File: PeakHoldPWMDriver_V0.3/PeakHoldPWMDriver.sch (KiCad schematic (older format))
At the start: 105 parts, among them J1 Screw_Terminal_01x06, J2 Screw_Terminal_01x08, Q1 AO3400, Q10 AO3400, Q11 2N7002, Q12 2N7002, Q13 TSM2309, Q14 IRLL 024N, Q15 TSM2309, Q16 IRLL 024N, Q2 AO3400, Q3 2N7002, Q4 2N7002, Q5 TSM2309, Q6 TSM2309, Q7 IRLL 024N, Q8 IRLL 024N, Q9 AO3400, U1 74LS32, U2 LM2901, U3 74LS74, U4 LTC6992, U5 74LS74, U6 LM78M05, U7 74LS08, U8 74LS08

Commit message: cleaup
cleanup of silkscreen
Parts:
- R3: value 500k -> 470k
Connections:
- net PWR_GND: now also RV1.1, RV2.1; no longer RV1.3, RV2.3
- net at D4.2 (A), R6.2: now also RV2.3; no longer RV2.1
- net at D1.2 (A), R2.2: now also RV1.3; no longer RV1.1
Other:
- moved on the sheet: D1, R2, RV2
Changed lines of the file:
@@
 L Device:R_Small R2
 U 1 1 5F079FC0
-P 1350 6300
-F 0 "R2" H 1409 6346 50  0000 L CNN
-F 1 "470R" H 1409 6255 50  0000 L CNN
-F 2 "Resistor_SMD:R_0603_1608Metric_Pad1.05x0.95mm_HandSolder" H 1350 6300 50  0001 C CNN
-F 3 "~" H 1350 6300 50  0001 C CNN
-	1    1350 6300
-	1    0    0    -1
-$EndComp
-Wire Wire Line
-	1350 6400 1350 6450
-Text GLabel 1250 6150 0    50   Input ~ 0
+P 1050 6800
+F 0 "R2" H 1109 6846 50  0000 L CNN
+F 1 "470R" H 1109 6755 50  0000 L CNN
+F 2 "Resistor_SMD:R_0603_1608Metric_Pad1.05x0.95mm_HandSolder" H 1050 6800 50  0001 C CNN
+F 3 "~" H 1050 6800 50  0001 C CNN
+	1    1050 6800
+	-1   0    0    1
+$EndComp
+Wire Wire Line
+	1050 6700 1050 6650
+Text GLabel 1150 6950 2    50   Input ~ 0
 5V
 Wire Wire Line
-	1250 6150 1350 6150
-Wire Wire Line
-	1350 6150 1350 6200
-Wire Wire Line
-	1350 6650 1350 6700
-Wire Wire Line
-	1350 6700 1250 6700
+	1150 6950 1050 6950
+Wire Wire Line
+	1050 6950 1050 6900
 $Comp
 L Device:R_POT_Small RV1
@@
 $EndComp
 Wire Wire Line
-	1350 6450 1700 6450
-Connection ~ 1350 6450
-Wire Wire Line
-	1350 6700 1550 6700
-Wire Wire Line
-	1700 6700 1700 6650
-Connection ~ 1350 6700
-Wire Wire Line
 	1800 6600 1800 6550
 $Comp
@@
 P 1750 6750
 F 0 "R3" H 1600 6800 42  0000 L BNN
-F 1 "500k" H 1600 6650 42  0000 L BNN
+F 1 "470k" H 1600 6650 42  0000 L BNN
 F 2 "Resistor_SMD:R_0603_1608Metric_Pad1.05x0.95mm_HandSolder" H 1750 6750 50  0001 C CNN
 F 3 "" H 1750 6750 50  0001 C CNN
@@
 Wire Wire Line
 	1900 6700 1900 6750
-Wire Wire Line
-	1600 6750 1550 6750
-Wire Wire Line
-	1550 6750 1550 6700
-Connection ~ 1550 6700
-Wire Wire Line
-	1550 6700 1700 6700
 $Comp
 L Speeduino_base-eagle-import:SMD-RES-470R-5%-1_10W(0603) R4
@@
 L Device:D_Schottky_Small D1
 U 1 1 5F079FBA
-P 1350 6550
-F 0 "D1" H 1350 6437 50  0000 C CNN
-F 1 "BAV103" V 1395 6618 50  0001 L CNN
-F 2 "Diode_SMD:D_MiniMELF" V 1350 6550 50  0001 C CNN
-F 3 "~" V 1350 6550 50  0001 C CNN
-	1    1350 6550
-	0    -1   -1   0
+P 1050 6550
+F 0 "D1" H 1050 6437 50  0000 C CNN
+F 1 "BAV103" V 1095 6618 50  0001 L CNN
+F 2 "Diode_SMD:D_MiniMELF" V 1050 6550 50  0001 C CNN
+F 3 "~" V 1050 6550 50  0001 C CNN
+	1    1050 6550
+	0    1    1    0
 $EndComp
 $Comp
@@
 Text GLabel 3050 6600 2    50   Output ~ 0
 PWM
-Text GLabel 3900 6750 2    50   Output ~ 0
+Text GLabel 3800 6750 0    50   Output ~ 0
 VREF
 Connection ~ 3450 6900
@@
 	3450 6900 3800 6900
 Connection ~ 3450 6650
-Wire Wire Line
-	3450 6650 3800 6650
 $Comp
 L Device:R_POT_Small RV2
 U 1 1 5EDE3906
-P 3800 6750
-F 0 "RV2" H 3741 6796 50  0000 R CNN
-F 1 "5K" H 3741 6705 50  0000 R CNN
-F 2 "Potentiometer_SMD:Potentiometer_Bourns_3314R-1_Vertical_Hole" H 3800 6750 50  0001 C CNN
-F 3 "~" H 3800 6750 50  0001 C CNN
-	1    3800 6750
-	1    0    0    -1
+P 3900 6750
+F 0 "RV2" H 3841 6796 50  0000 R CNN
+F 1 "5K" H 3841 6705 50  0000 R CNN
+F 2 "Potentiometer_SMD:Potentiometer_Bourns_3314R-1_Vertical_Hole" H 3900 6750 50  0001 C CNN
+F 3 "~" H 3900 6750 50  0001 C CNN
+	1    3900 6750
+	-1   0    0    1
 $EndComp
 Wire Wire Line
@@
 Text GLabel 3350 6900 0    50   Input ~ 0
 PWR_GND
-Text GLabel 1250 6700 0    50   Input ~ 0
+Text GLabel 1050 6350 1    50   Input ~ 0
 PWR_GND
 Text GLabel 4400 5200 2    50   Input ~ 0
@@
 Wire Wire Line
 	10000 4500 10050 4500
+Wire Wire Line
+	3450 6650 3900 6650
+Wire Wire Line
+	3800 6850 3900 6850
+Text GLabel 1550 6800 3    50   Input ~ 0
+PWR_GND
+Wire Wire Line
+	1550 6800 1550 6750
+Wire Wire Line
+	1550 6750 1600 6750
+Wire Wire Line
+	1050 6350 1050 6400
+Wire Wire Line
+	1050 6400 1700 6400
+Wire Wire Line
+	1700 6400 1700 6450
+Connection ~ 1050 6400
+Wire Wire Line
+	1050 6400 1050 6450
+Wire Wire Line
+	1050 6650 1700 6650
+Connection ~ 1050 6650
 $EndSCHEMATC

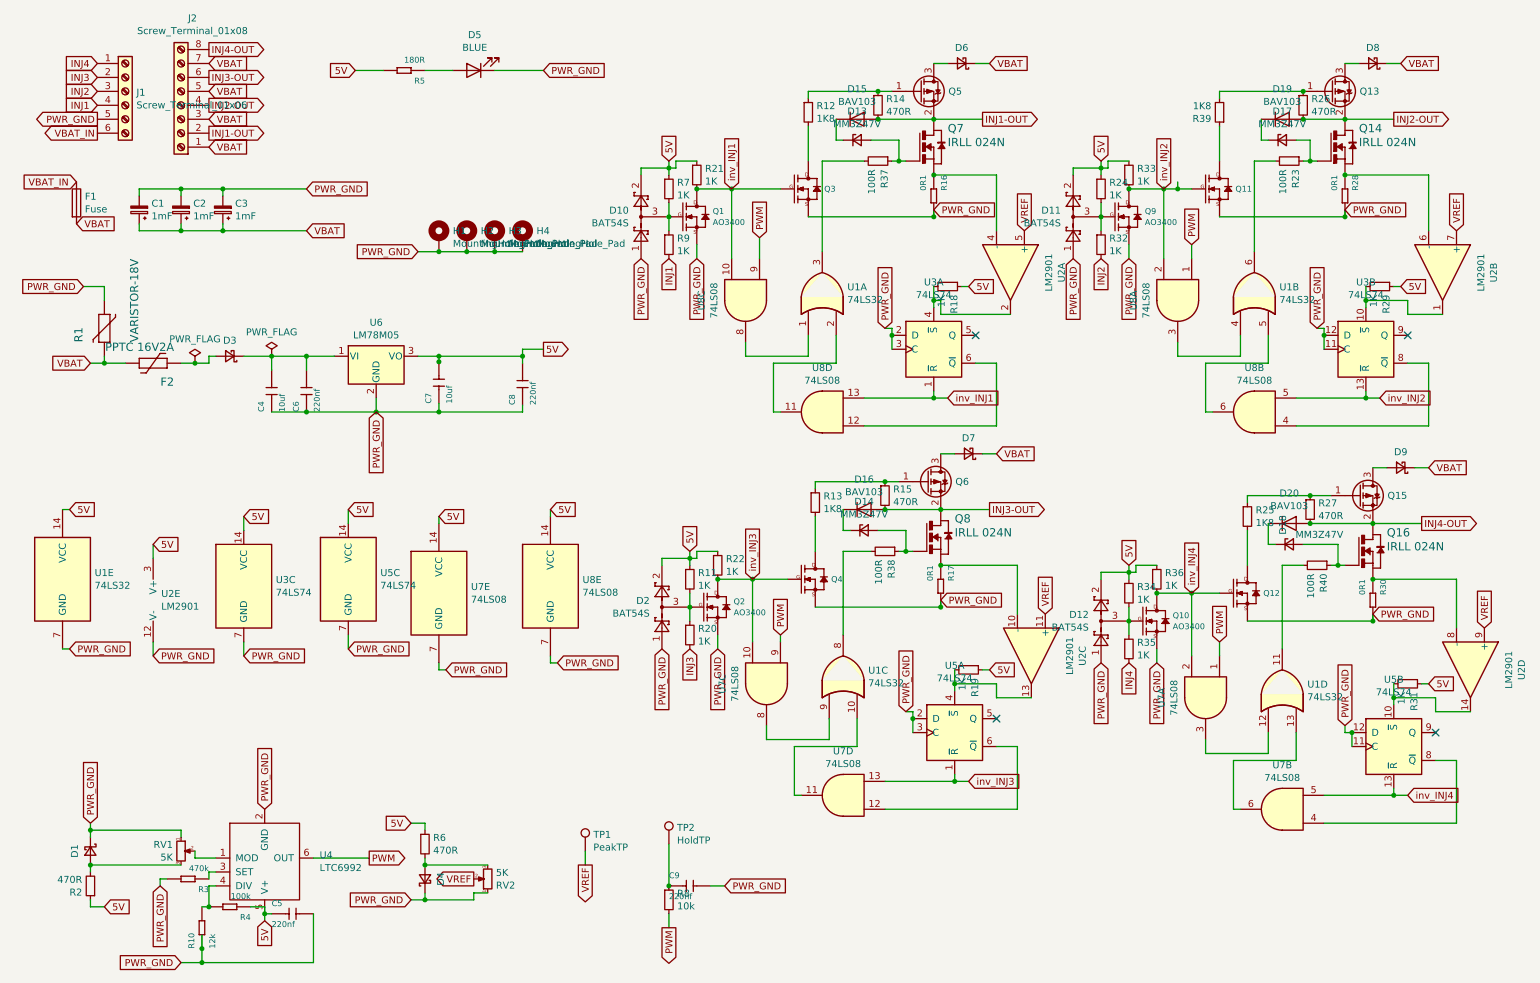
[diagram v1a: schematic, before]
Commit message: Added jumpers to choose between ECU or transistor input
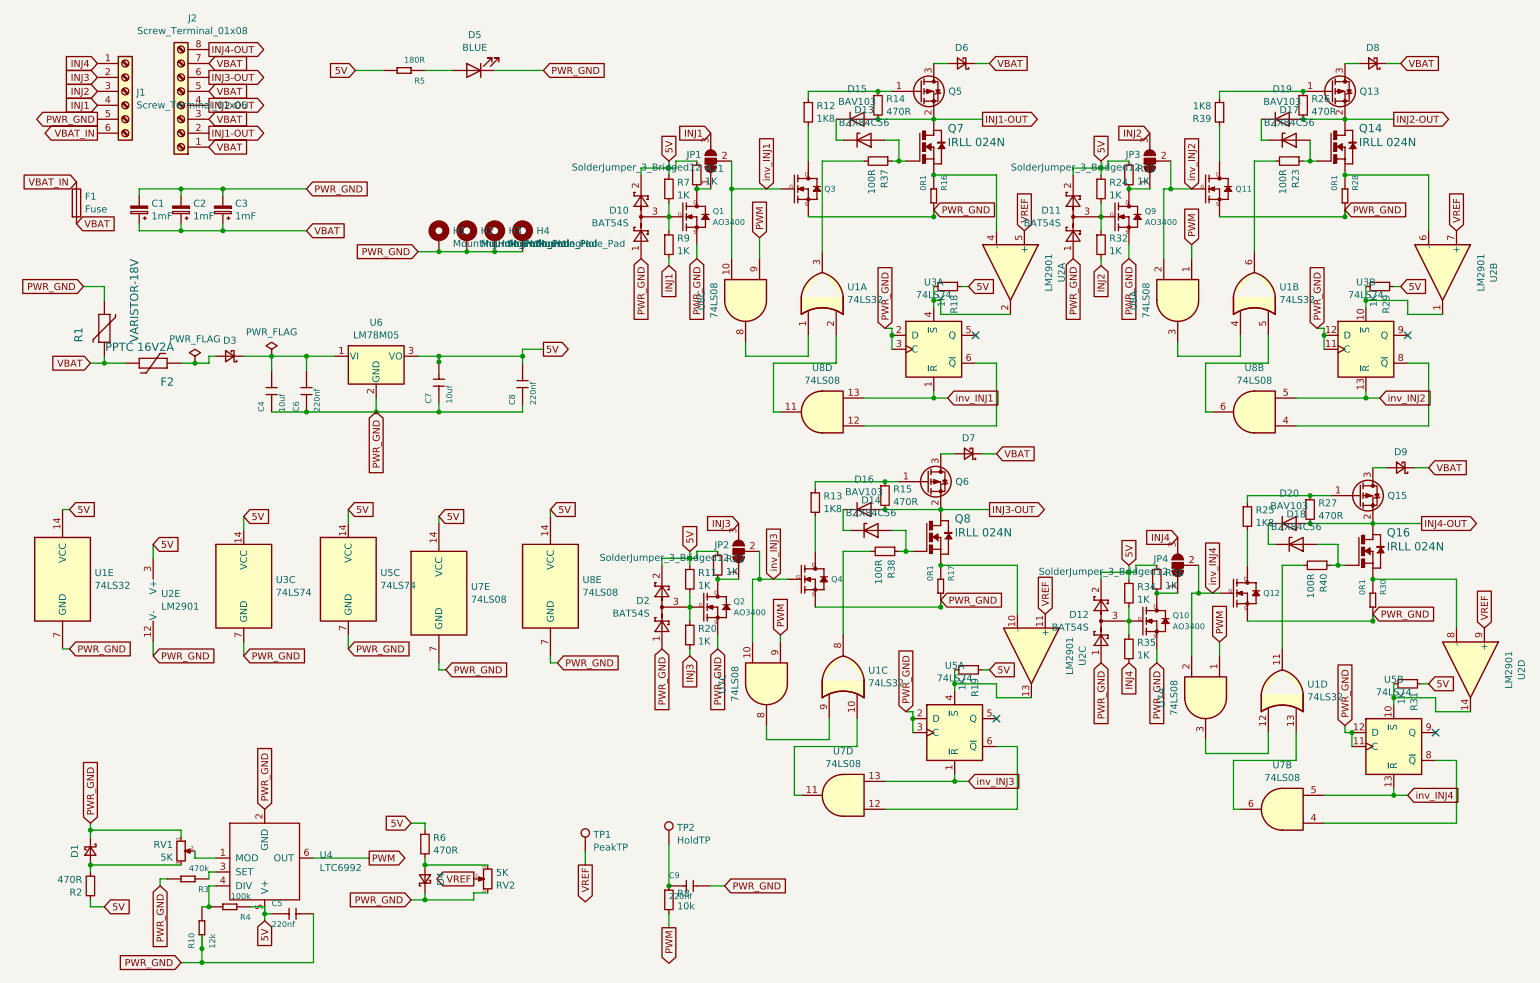
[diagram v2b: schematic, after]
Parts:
- removed D13, D14, D17, D18: MM3Z47V, Diode_SMD:D_SOD-323, symbol Device:D_Zener_Small
- added D13, D14, D17, D18: BZX84C56, Diode_SMD:D_SOT-23_ANK, symbol Diode:BZX84Cxx
- added JP1, JP2, JP3, JP4: SolderJumper_3_Bridged12, Jumper:SolderJumper-3_P1.3mm_Bridged12_Pad1.0x1.5mm, symbol Jumper:SolderJumper_3_Bridged12
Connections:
- net INJ1: now also JP1.3 (B)
- net INJ2: now also JP3.3 (B)
- net INJ3: now also JP2.3 (B)
- net INJ4: now also JP4.3 (B)
- net inv_INJ1: now also JP1.2 (C); no longer Q1.3 (D), R21.2
- net inv_INJ2: now also JP3.2 (C); no longer Q9.3 (D), R33.2
- net inv_INJ3: now also JP2.2 (C); no longer Q2.3 (D), R22.2
- net inv_INJ4: now also JP4.2 (C); no longer Q10.3 (D), R36.2
- net at Q8.1 (G), R38.1: now also D14.2 (A)
- net at Q14.1 (G), R23.1: now also D17.2 (A)
- net at Q16.1 (G), R40.1: now also D18.2 (A)
- net at Q7.1 (G), R37.1: now also D13.2 (A)
- net at D16.1 (K): now also D14.1 (K)
- net at D15.1 (K): now also D13.1 (K)
- net at D19.1 (K): now also D17.1 (K)
- net at D20.1 (K): now also D18.1 (K)
- new net: JP1.1 (A), Q1.3 (D), R21.2
- new net: JP2.1 (A), Q2.3 (D), R22.2
- new net: JP4.1 (A), Q10.3 (D), R36.2
- new net: JP3.1 (A), Q9.3 (D), R33.2
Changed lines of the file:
@@
 Wire Wire Line
 	6200 1150 6200 1100
-Text GLabel 5650 1800 1    50   Input ~ 0
+Text GLabel 5900 1800 1    50   Input ~ 0
 inv_INJ1
 Wire Wire Line
@@
 Wire Wire Line
 	6250 3950 6250 3900
-Text GLabel 5800 4600 1    50   Input ~ 0
+Text GLabel 5950 4600 1    50   Input ~ 0
 inv_INJ3
 Text GLabel 10050 1950 2    50   Input ~ 0
@@
 Wire Wire Line
 	9150 1100 9750 1100
-Wire Wire Line
-	8850 1750 8850 1800
-Wire Wire Line
-	8850 1800 8950 1800
-Wire Wire Line
-	8850 1800 8750 1800
-Connection ~ 8850 1800
-Text GLabel 8750 1800 1    50   Input ~ 0
+Text GLabel 8950 1800 1    50   Input ~ 0
 inv_INJ2
 Text GLabel 10250 4850 2    50   Input ~ 0
@@
 Wire Wire Line
 	9350 4050 9350 4000
-Text GLabel 8950 4700 1    50   Input ~ 0
+Text GLabel 9100 4700 1    50   Input ~ 0
 inv_INJ4
 Text GLabel 10450 900  2    50   Input ~ 0
@@
 Text GLabel 5000 2300 3    50   Input ~ 0
 PWR_GND
-Text GLabel 5200 2300 3    50   Input ~ 0
-INJ1
 Text GLabel 1100 1200 0    50   Input ~ 0
 INJ1
@@
 	1850 7350 2650 7350
 Wire Wire Line
-	5800 4600 6050 4600
+	5800 4600 5850 4600
 Wire Wire Line
 	5650 1800 6000 1800
@@
 	5400 2200 5400 2300
 Wire Wire Line
-	5400 1800 5650 1800
-Wire Wire Line
 	5200 2000 5200 2100
 Wire Wire Line
@@
 	1    0    0    -1
 $EndComp
-Connection ~ 5650 1800
 Wire Wire Line
 	5000 1700 5000 1650
@@
 	8950 4700 8950 5150
 Wire Wire Line
-	8950 4700 9150 4700
+	8950 4700 9000 4700
 $Comp
 L Device:R_Small R21
@@
 	1    0    0    -1
 $EndComp
-Connection ~ 5400 1800
 Wire Wire Line
 	5400 1600 5250 1600
@@
 Text GLabel 5150 5100 3    50   Input ~ 0
 PWR_GND
-Text GLabel 5350 5100 3    50   Input ~ 0
+Text GLabel 5350 5150 3    50   Input ~ 0
 INJ3
 $Comp
@@
 	5550 5000 5550 5100
 Wire Wire Line
-	5550 4600 5800 4600
-Wire Wire Line
 	5350 4800 5350 4900
 Wire Wire Line
@@
 	1    0    0    -1
 $EndComp
-Connection ~ 5550 4600
 Wire Wire Line
 	5550 4400 5400 4400
@@
 	1    0    0    -1
 $EndComp
-Connection ~ 5800 4600
 Text GLabel 8300 5200 3    50   Input ~ 0
 PWR_GND
@@
 	8700 5100 8700 5200
 Wire Wire Line
-	8700 4700 8950 4700
-Wire Wire Line
 	8500 4900 8500 5000
 Wire Wire Line
@@
 	1    0    0    -1
 $EndComp
-Connection ~ 8700 4700
 Wire Wire Line
 	8700 4500 8550 4500
@@
 	1    0    0    -1
 $EndComp
-Connection ~ 8950 4700
 Wire Wire Line
 	8750 1800 8750 2300
 Text GLabel 8100 2300 3    50   Input ~ 0
 PWR_GND
-Text GLabel 8300 2300 3    50   Input ~ 0
+Text GLabel 8300 2350 3    50   Input ~ 0
 INJ2
 $Comp
@@
 	8500 2200 8500 2300
 Wire Wire Line
-	8500 1800 8750 1800
-Wire Wire Line
 	8300 2000 8300 2100
 Wire Wire Line
@@
 	1    0    0    -1
 $EndComp
-Connection ~ 8500 1800
 Wire Wire Line
 	8500 1600 8350 1600
@@
 Wire Wire Line
 	8350 1650 8300 1650
-$Comp
-L Device:R_Small R32
-U 1 1 5F5596E1
-P 8300 2200
-F 0 "R32" H 8359 2246 50  0000 L CNN
-F 1 "1K" H 8359 2155 50  0000 L CNN
-F 2 "Resistor_SMD:R_0603_1608Metric_Pad1.05x0.95mm_HandSolder" H 8300 2200 50  0001 C CNN
-F 3 "~" H 8300 2200 50  0001 C CNN
-	1    8300 2200
-	1    0    0    -1
-$EndComp
-Connection ~ 8750 1800
 $Comp
 L Device:R_Small R39
@@
 Connection ~ 6750 4100
 $Comp
-L Device:D_Zener_Small D14
-U 1 1 5F6A39A6
-P 6600 4250
-F 0 "D14" H 6600 4457 50  0000 C CNN
-F 1 "MM3Z47V" H 6600 4366 50  0000 C CNN
-F 2 "Diode_SMD:D_SOD-323" V 6600 4250 50  0001 C CNN
-F 3 "~" V 6600 4250 50  0001 C CNN
-	1    6600 4250
-	1    0    0    -1
-$EndComp
-$Comp
 L Diode:BAV19 D15
 U 1 1 5F6E7FDD
@@
 $EndComp
 $Comp
-L Device:D_Zener_Small D13
-U 1 1 5F6E7FE3
-P 6550 1450
-F 0 "D13" H 6550 1657 50  0000 C CNN
-F 1 "MM3Z47V" H 6550 1566 50  0000 C CNN
-F 2 "Diode_SMD:D_SOD-323" V 6550 1450 50  0001 C CNN
-F 3 "~" V 6550 1450 50  0001 C CNN
-	1    6550 1450
-	1    0    0    -1
-$EndComp
-$Comp
 L Diode:BAV19 D19
 U 1 1 5F702F08
@@
 	1    0    0    -1
 $EndComp
-$Comp
-L Device:D_Zener_Small D18
-U 1 1 5F73AD7B
-P 9650 4350
-F 0 "D18" V 9604 4420 50  0000 L CNN
-F 1 "MM3Z47V" H 9695 4420 50  0000 L CNN
-F 2 "Diode_SMD:D_SOD-323" V 9650 4350 50  0001 C CNN
-F 3 "~" V 9650 4350 50  0001 C CNN
-	1    9650 4350
-	1    0    0    -1
-$EndComp
 Connection ~ 9750 1300
 Connection ~ 6700 1300
 Connection ~ 9800 4200
 Wire Wire Line
-	6650 1450 6850 1450
-Wire Wire Line
 	6850 1450 6850 1600
 Connection ~ 6850 1600
@@
 Wire Wire Line
 	6300 1600 6600 1600
-$Comp
-L Device:D_Zener_Small D17
-U 1 1 5F702F0E
-P 9600 1450
-F 0 "D17" H 9600 1657 50  0000 C CNN
-F 1 "MM3Z47V" H 9600 1566 50  0000 C CNN
-F 2 "Diode_SMD:D_SOD-323" V 9600 1450 50  0001 C CNN
-F 3 "~" V 9600 1450 50  0001 C CNN
-	1    9600 1450
-	1    0    0    -1
-$EndComp
 Wire Wire Line
 	9400 1600 9550 1600
@@
 Wire Wire Line
 	9450 1300 9450 1450
-Wire Wire Line
-	9700 1450 9800 1450
 Wire Wire Line
 	9800 1450 9800 1600
@@
 	6450 4400 6450 5000
 Wire Wire Line
-	6700 4250 6900 4250
-Wire Wire Line
 	9500 4350 9550 4350
 Wire Wire Line
 	9500 4200 9500 4350
-Wire Wire Line
-	9750 4350 10000 4350
 Wire Wire Line
 	10000 4350 10000 4500
@@
 	1050 6650 1700 6650
 Connection ~ 1050 6650
+$Comp
+L Diode:BZX84Cxx D13
+U 1 1 5F25156C
+P 6600 1450
+F 0 "D13" H 6600 1667 50  0000 C CNN
+F 1 "BZX84C56" H 6600 1576 50  0000 C CNN
+F 2 "Diode_SMD:D_SOT-23_ANK" H 6600 1275 50  0001 C CNN
+F 3 "https://diotec.com/tl_files/diotec/files/pdf/datasheets/bzx84c2v4.pdf" H 6600 1450 50  0001 C CNN
+	1    6600 1450
+	1    0    0    -1
+$EndComp
+Wire Wire Line
+	6750 1450 6850 1450
+$Comp
+L Diode:BZX84Cxx D17
+U 1 1 5F292622
+P 9650 1450
+F 0 "D17" H 9650 1667 50  0000 C CNN
+F 1 "BZX84C56" H 9650 1576 50  0000 C CNN
+F 2 "Diode_SMD:D_SOT-23_ANK" H 9650 1275 50  0001 C CNN
+F 3 "https://diotec.com/tl_files/diotec/files/pdf/datasheets/bzx84c2v4.pdf" H 9650 1450 50  0001 C CNN
+	1    9650 1450
+	1    0    0    -1
+$EndComp
+$Comp
+L Diode:BZX84Cxx D14
+U 1 1 5F2A1B1C
+P 6650 4250
+F 0 "D14" H 6650 4467 50  0000 C CNN
+F 1 "BZX84C56" H 6650 4376 50  0000 C CNN
+F 2 "Diode_SMD:D_SOT-23_ANK" H 6650 4075 50  0001 C CNN
+F 3 "https://diotec.com/tl_files/diotec/files/pdf/datasheets/bzx84c2v4.pdf" H 6650 4250 50  0001 C CNN
+	1    6650 4250
+	1    0    0    -1
+$EndComp
+$Comp
+L Diode:BZX84Cxx D18
+U 1 1 5F2A3132
+P 9700 4350
+F 0 "D18" H 9700 4567 50  0000 C CNN
+F 1 "BZX84C56" H 9700 4476 50  0000 C CNN
+F 2 "Diode_SMD:D_SOT-23_ANK" H 9700 4175 50  0001 C CNN
+F 3 "https://diotec.com/tl_files/diotec/files/pdf/datasheets/bzx84c2v4.pdf" H 9700 4350 50  0001 C CNN
+	1    9700 4350
+	1    0    0    -1
+$EndComp
+Wire Wire Line
+	6800 4250 6900 4250
+Wire Wire Line
+	9850 4350 10000 4350
+Text GLabel 5200 2350 3    50   Input ~ 0
+INJ1
+$Comp
+L Device:R_Small R32
+U 1 1 5F5596E1
+P 8300 2200
+F 0 "R32" H 8359 2246 50  0000 L CNN
+F 1 "1K" H 8359 2155 50  0000 L CNN
+F 2 "Resistor_SMD:R_0603_1608Metric_Pad1.05x0.95mm_HandSolder" H 8300 2200 50  0001 C CNN
+F 3 "~" H 8300 2200 50  0001 C CNN
+	1    8300 2200
+	1    0    0    -1
+$EndComp
+Wire Wire Line
+	5200 2300 5200 2350
+Wire Wire Line
+	8300 2300 8300 2350
+Wire Wire Line
+	5350 5100 5350 5150
+Wire Wire Line
+	8750 1800 8800 1800
+$Comp
+L Jumper:SolderJumper_3_Bridged12 JP2
+U 1 1 5F5DA522
+P 5700 4400
+F 0 "JP2" V 5746 4468 50  0000 L CNN
+F 1 "SolderJumper_3_Bridged12" V 5655 4468 50  0000 L CNN
+F 2 "Jumper:SolderJumper-3_P1.3mm_Bridged12_Pad1.0x1.5mm" H 5700 4400 50  0001 C CNN
+F 3 "~" H 5700 4400 50  0001 C CNN
+	1    5700 4400
+	0    -1   -1   0
+$EndComp
+Wire Wire Line
+	5550 4600 5700 4600
+Connection ~ 5550 4600
+Wire Wire Line
+	5850 4400 5850 4600
+Connection ~ 5850 4600
+Wire Wire Line
+	5850 4600 6050 4600
+Text GLabel 5700 4200 0    50   Input ~ 0
+INJ3
+$Comp
+L Jumper:SolderJumper_3_Bridged12 JP1
+U 1 1 5F632981
+P 5500 1600
+F 0 "JP1" V 5546 1668 50  0000 L CNN
+F 1 "SolderJumper_3_Bridged12" V 5455 1668 50  0000 L CNN
+F 2 "Jumper:SolderJumper-3_P1.3mm_Bridged12_Pad1.0x1.5mm" H 5500 1600 50  0001 C CNN
+F 3 "~" H 5500 1600 50  0001 C CNN
+	1    5500 1600
+	0    -1   -1   0
+$EndComp
+$Comp
+L Jumper:SolderJumper_3_Bridged12 JP3
+U 1 1 5F634156
+P 8650 1600
+F 0 "JP3" V 8696 1668 50  0000 L CNN
+F 1 "SolderJumper_3_Bridged12" V 8605 1668 50  0000 L CNN
+F 2 "Jumper:SolderJumper-3_P1.3mm_Bridged12_Pad1.0x1.5mm" H 8650 1600 50  0001 C CNN
+F 3 "~" H 8650 1600 50  0001 C CNN
+	1    8650 1600
+	0    -1   -1   0
+$EndComp
+$Comp
+L Jumper:SolderJumper_3_Bridged12 JP4
+U 1 1 5F635F7F
+P 8850 4500
+F 0 "JP4" V 8896 4568 50  0000 L CNN
+F 1 "SolderJumper_3_Bridged12" V 8805 4568 50  0000 L CNN
+F 2 "Jumper:SolderJumper-3_P1.3mm_Bridged12_Pad1.0x1.5mm" H 8850 4500 50  0001 C CNN
+F 3 "~" H 8850 4500 50  0001 C CNN
+	1    8850 4500
+	0    -1   -1   0
+$EndComp
+Wire Wire Line
+	8850 4700 8700 4700
+Connection ~ 8700 4700
+Wire Wire Line
+	8650 1800 8500 1800
+Connection ~ 8500 1800
+Wire Wire Line
+	5500 1800 5400 1800
+Connection ~ 5400 1800
+Wire Wire Line
+	5650 1600 5650 1800
+Connection ~ 5650 1800
+Wire Wire Line
+	8800 1600 8800 1800
+Connection ~ 8800 1800
+Wire Wire Line
+	8800 1800 8950 1800
+Wire Wire Line
+	9000 4500 9000 4700
+Connection ~ 9000 4700
+Wire Wire Line
+	9000 4700 9150 4700
+Text GLabel 8850 4300 0    50   Input ~ 0
+INJ4
+Text GLabel 8650 1400 0    50   Input ~ 0
+INJ2
+Text GLabel 5500 1400 0    50   Input ~ 0
+INJ1
 $EndSCHEMATC

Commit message: Updates on V0.3
Updated V0.3
- Created readme
- Cleaned up baord.
- Created gerbers
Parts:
- Q1, Q10, Q2, Q9: value AO3400 -> 2N7002
- Q11, Q12, Q3, Q4: footprint Package_TO_SOT_SMD:SOT-23_Handsoldering -> Package_TO_SOT_SMD:SOT-23
- renumbered D14 to D10, D6 to D11, D7 to D12, D11 to D13, D12 to D14, D19 to D15, D17 to D16, D20 to D17, D8 to D19, D3 to D2, D9 to D20, D4 to D3, D5 to D4, D10 to D5, D2 to D6, D15 to D7, D13 to D8, D16 to D9, R2 to R1, R8 to R10, R20 to R12, R21 to R13, R22 to R14, R12 to R15, R13 to R16, R14 to R17, R37 to R18, R15 to R19, R1 to R2, R38 to R20, R16 to R21, R17 to R22, R18 to R23, R19 to R24, R24 to R25, R32 to R26, R33 to R27, R34 to R28, R35 to R29, R36 to R30, R39 to R31, R25 to R32, R23 to R33, R26 to R34, R27 to R35, R40 to R36, R28 to R37, R30 to R38, R29 to R39, R10 to R4, R31 to R40, R4 to R5, R5 to R6, R6 to R7, R7 to R8
